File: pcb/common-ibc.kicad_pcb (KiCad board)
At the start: 4 copper layers, 67 x 65 mm, 103 parts, among them J1 XILINX_JTAG, J10 U.FL, J11 MOLEX_0039291087, J2 MOLEX_0039291067, J3 GROUND, J4 GROUND, J5 MOLEX_0532610571, J6 U.FL, J7 U.FL, J8 U.FL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

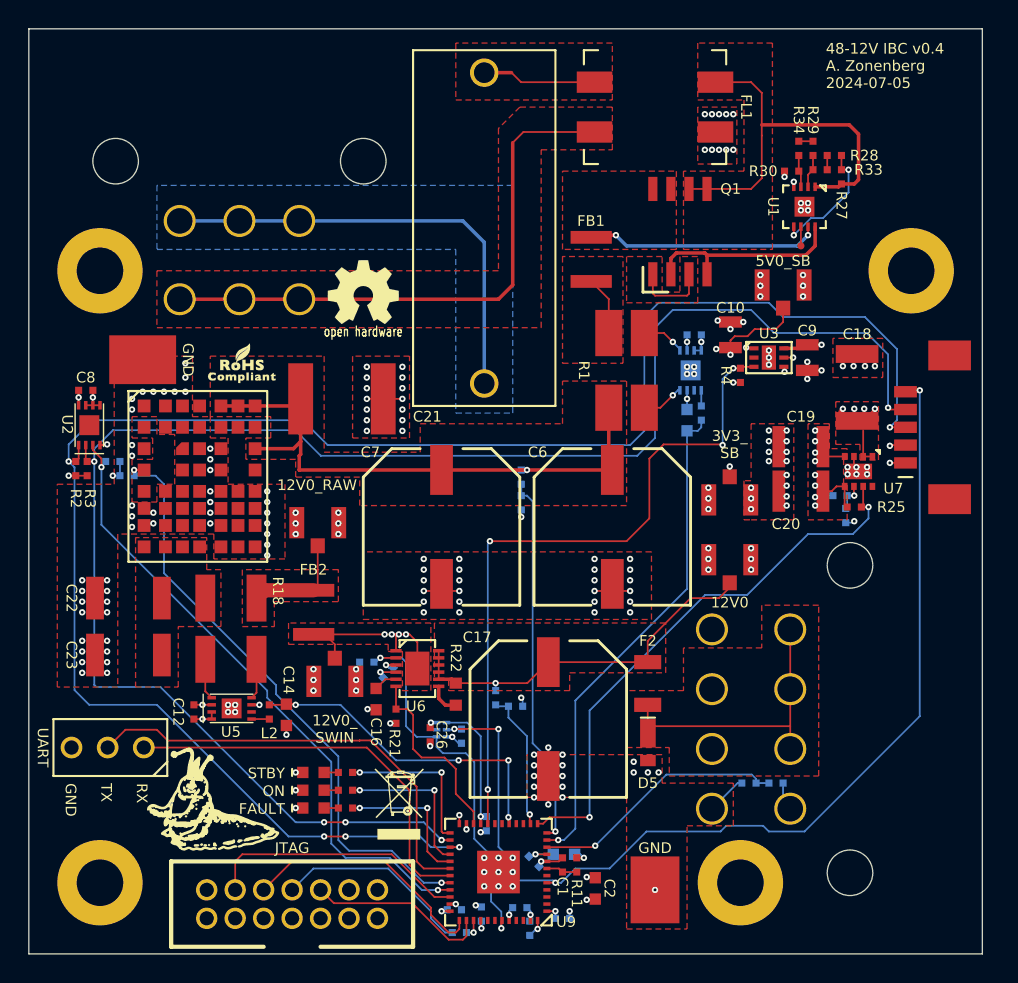
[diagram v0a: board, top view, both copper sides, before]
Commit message: Finished layout review on IBC, made some tweaks to routing and solder paste
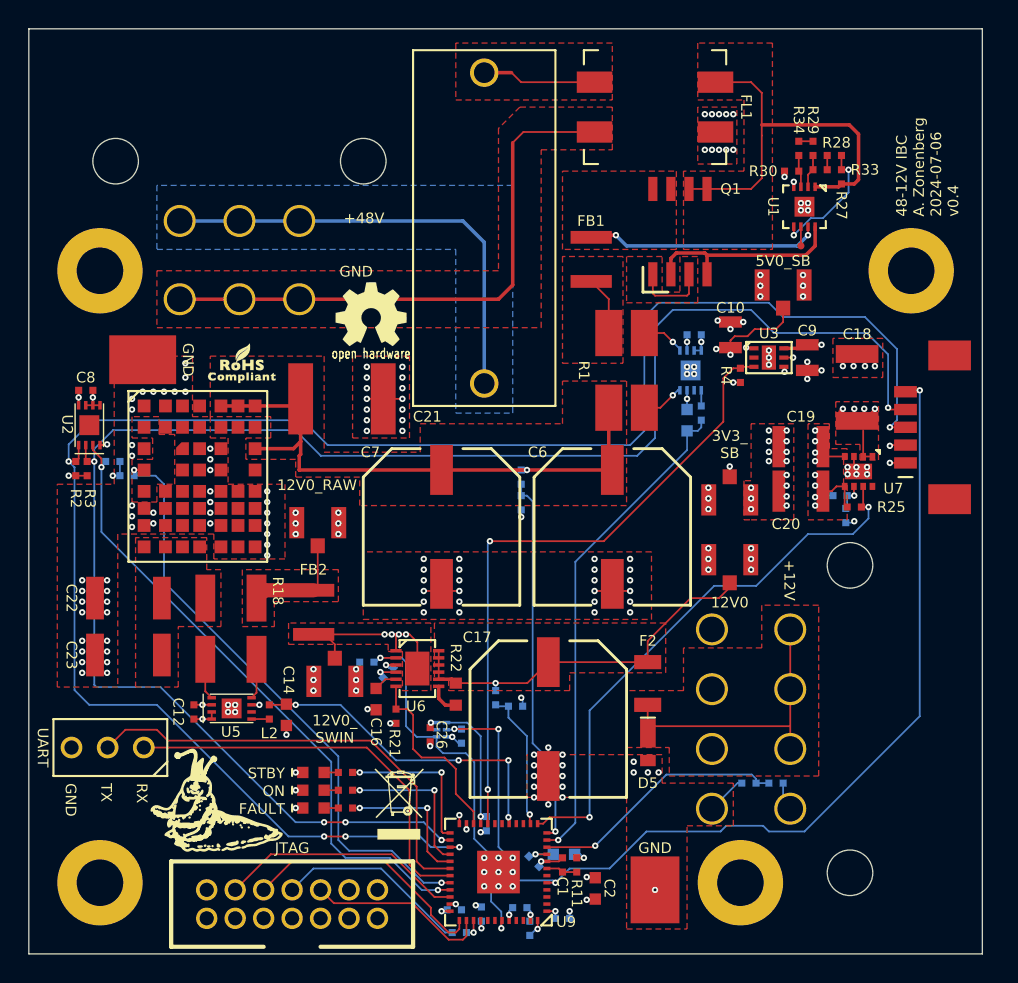
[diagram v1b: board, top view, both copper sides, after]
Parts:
- moved M2 1.64 mm to (58.0, 40.0)
- moved M1 0.26 mm to (47.7, 74.6)
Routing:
- net /5V0_SB_PGOOD: track 48.5 -> 45.2 mm, vias 4 -> 2
- net /JTAG_TMS: track 18.5 -> 17.4 mm
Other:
- board text added: "+12V"
- board text added: "+48V"
- board text added: "48-12V IBC A. Zonenberg 2024-07-06 v0.4"
- board text added: "Place UL mark and date code in this area"
- board text removed: "48-12V IBC v0.4 A. Zonenberg 2024-07-05"
